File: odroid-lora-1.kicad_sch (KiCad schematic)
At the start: 14 parts, among them J1 ODROID_2x12_GPIO, J2 RASPPI_2x20_GPIO, J3 M0, J4 M1

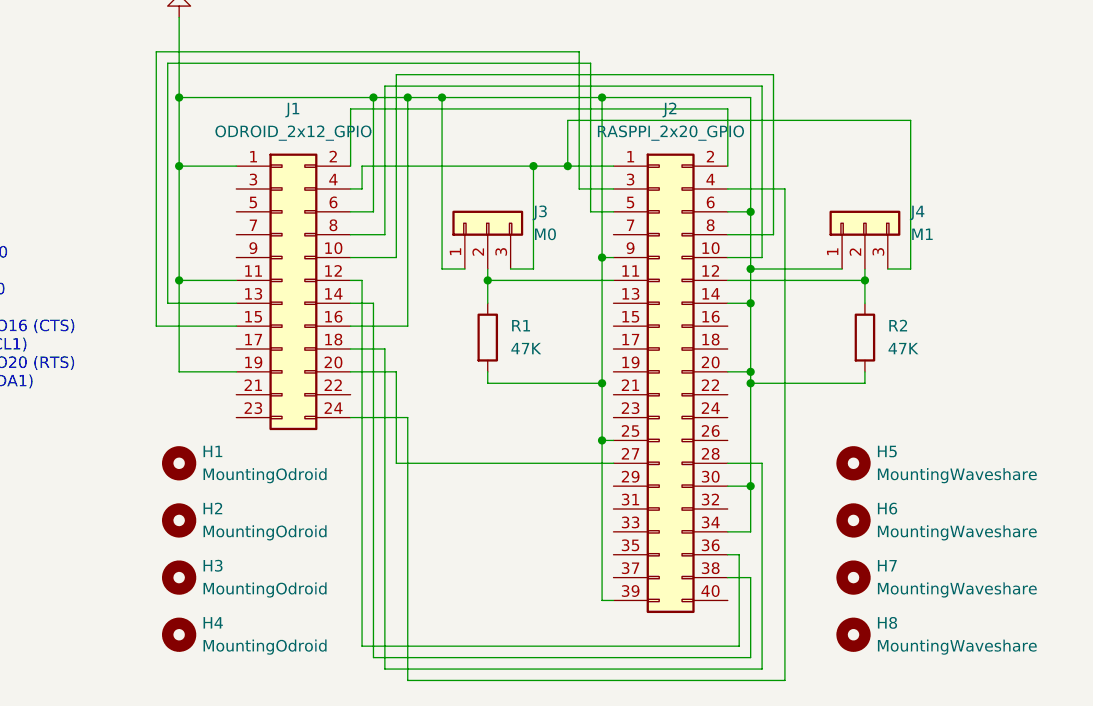
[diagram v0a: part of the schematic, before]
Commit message: update to angled condensed design
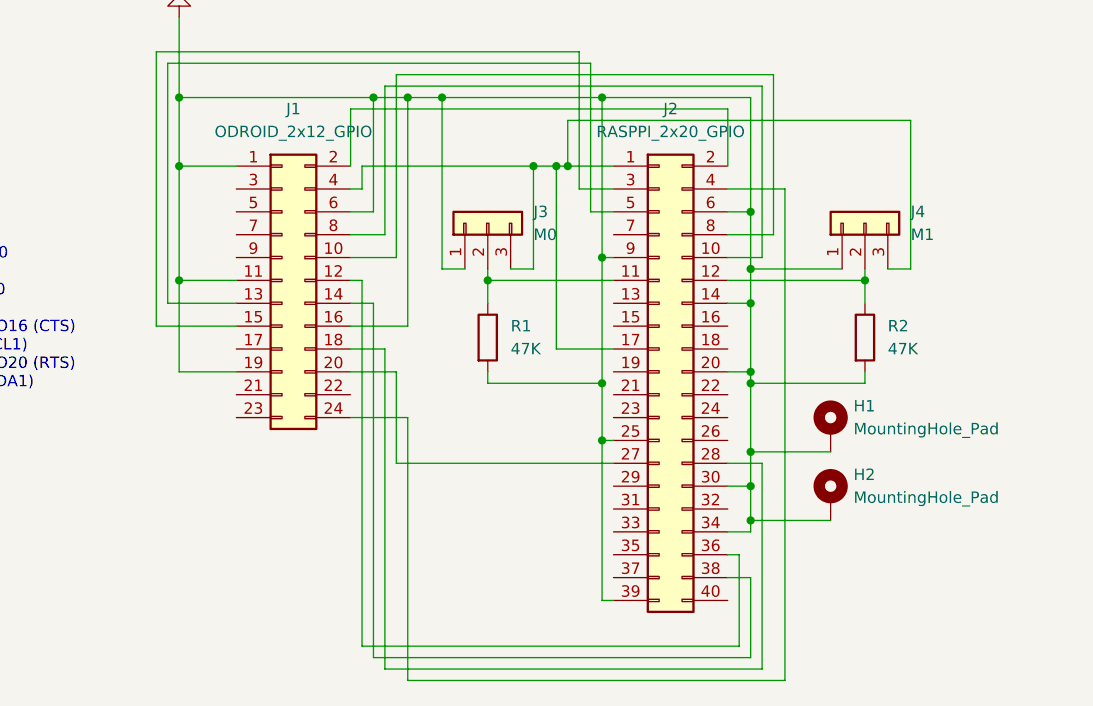
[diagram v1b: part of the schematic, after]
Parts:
- removed H1, H2, H3, H4: MountingOdroid, MountingHole:MountingHole_3.5mm_Pad, symbol Mechanical:MountingHole
- removed H5, H6, H7, H8: MountingWaveshare, MountingHole:MountingHole_3.5mm_Pad, symbol Mechanical:MountingHole
- added H1, H2: MountingHole_Pad, MountingHole:MountingHole_3.5mm_Pad, symbol Mechanical:MountingHole_Pad
- J1: footprint Connector_PinHeader_2.54mm:PinHeader_2x12_P2.54mm_Vertical -> Connector_PinHeader_2.54mm:PinHeader_2x12_P2.54mm_Horizontal
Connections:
- net GND: now also H1.1, H2.1
- net at J1.4 (Pin_4), J2.1 (Pin_1), J3.3 (Pin_3)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: now also J2.17 (Pin_17)

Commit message: replace pinheader with pinsocket for the odroid connector
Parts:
- J1: footprint Connector_PinHeader_2.54mm:PinHeader_2x12_P2.54mm_Horizontal -> Connector_PinSocket_2.54mm:PinSocket_2x12_P2.54mm_Horizontal
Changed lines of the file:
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@@
 			)
 		)
-		(property "Footprint" "Connector_PinHeader_2.54mm:PinHeader_2x12_P2.54mm_Horizontal"
+		(property "Footprint" "Connector_PinSocket_2.54mm:PinSocket_2x12_P2.54mm_Horizontal"
 			(at 116.84 78.74 0)
 			(effects

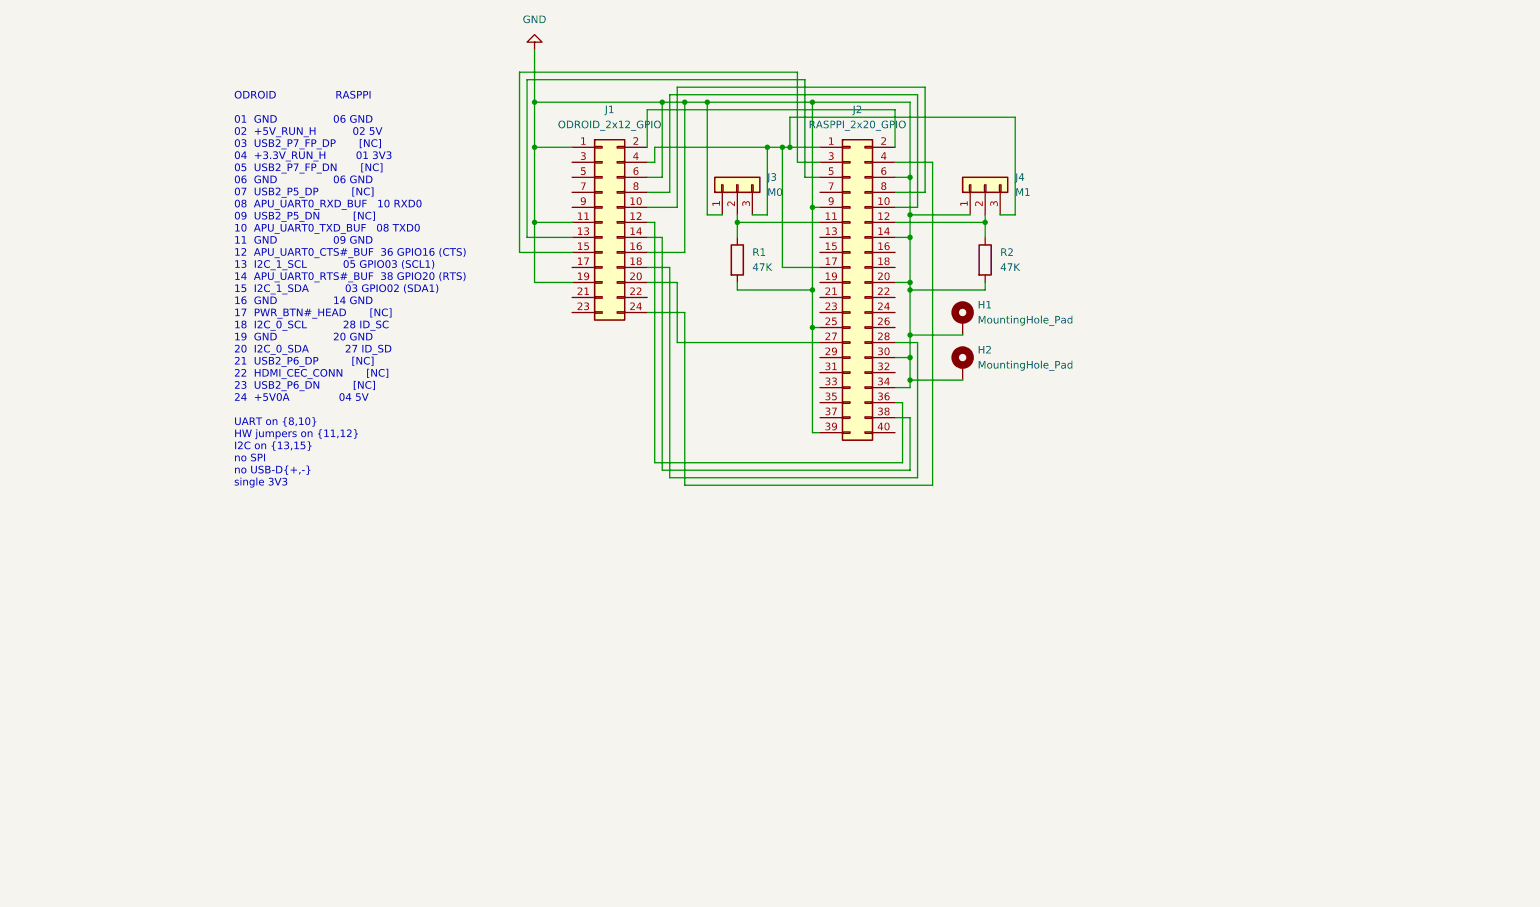
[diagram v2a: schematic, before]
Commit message: define power nets and increase trace width for currents
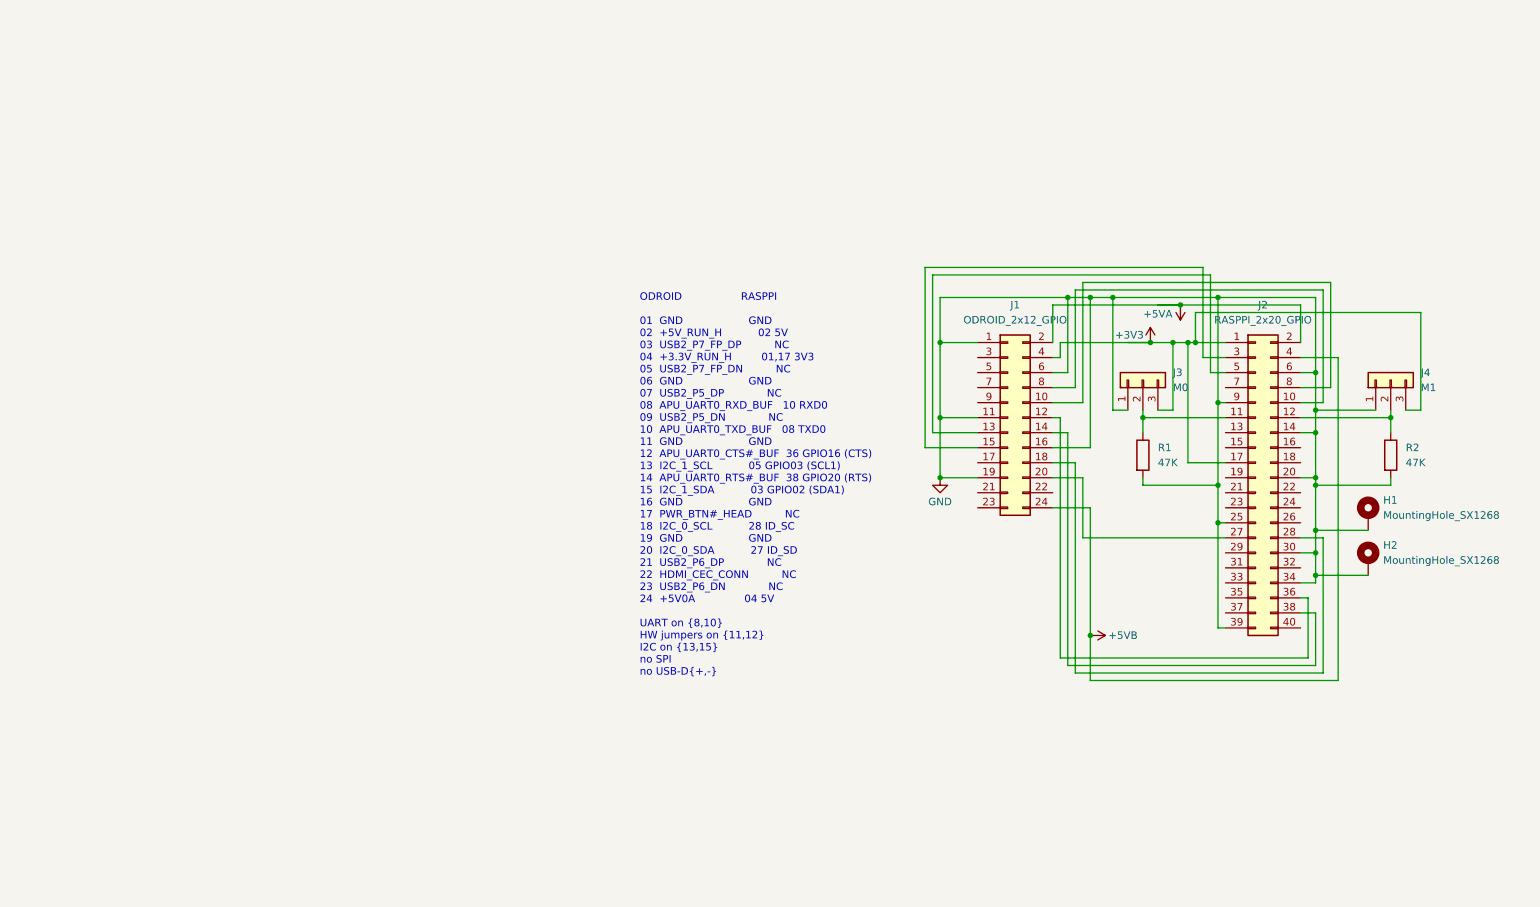
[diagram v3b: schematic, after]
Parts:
- H1, H2: value MountingHole_Pad -> MountingHole_SX1268
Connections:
- net +3V3: now reaches J1.4 (Pin_4), J2.1 (Pin_1), J2.17 (Pin_17), J3.3 (Pin_3), J4.3 (Pin_3)
- net +5VA: now reaches J1.2 (Pin_2), J2.2 (Pin_2)
- net +5VB: now reaches J1.24 (Pin_24), J2.4 (Pin_4)
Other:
- note added: "ODROID RASPPI 01 GND GND 02 +5V_RUN_H 02 5V 03 USB2_P7_FP_DP NC 04 +3.3V_RUN_H 01,17 3V3 05 USB2_P7_FP_DN NC 06 GND GND 07 USB2_P5_DP NC 08 APU_UART0_RXD_BUF 10 RXD0 09 USB2_P5_DN NC 10 APU_UART0_TXD_BUF 08 TXD0 11 GND GND 12 APU_UART0_CTS#_BUF 36 GPIO16 (CTS) 13 I2C_1_SCL 05 GPIO03 (SCL1) 14 APU_UART0_RTS#_BUF 38 GPIO20 (RTS) 15 I2C_1_SDA 03 GPIO02 (SDA1) 16 GND GND 17 PWR_BTN#_HEAD NC 18 I2C_0_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"
- note removed: "ODROID RASPPI 01 GND 06 GND 02 +5V_RUN_H 02 5V 03 USB2_P7_FP_DP [NC] 04 +3.3V_RUN_H 01 3V3 05 USB2_P7_FP_DN [NC] 06 GND 06 GND 07 USB2_P5_DP [NC] 08 APU_UART0_RXD_BUF 10 RXD0 09 USB2_P5_DN [NC] 10 APU_UART0_TXD_BUF 08 TXD0 11 GND 09 GND 12 APU_UART0_CTS#_BUF 36 GPIO16 (CTS) 13 I2C_1_SCL 05 GPIO03 (SCL1) 14 APU_UART0_RTS#_BUF 38 GPIO20 (RTS) 15 I2C_1_SDA 03 GPIO02 (SDA1) 16 GND 14 GND 17 PWR_BTN#_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"
- company: (none) -> l5yth
- title: (none) -> odroid-h3-sx1268-lora-hat
- moved on the sheet: H1, H2, J1, J2, J3, J4, R1, R2

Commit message: add fuses
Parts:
- added F1, F2: Fuse_2A, Fuse:Fuse_1206_3216Metric, symbol Device:Fuse
- H1, H2: value MountingHole_SX1268 -> MOUNT_SX1268
- J1: value ODROID_2x12_GPIO -> ODROID_2x12_SOCKET
- J2: value RASPPI_2x20_GPIO -> RASPPI_2x20_HEADER
- J3: value M0 -> Mode0
- J4: value M1 -> Mode1
- R1, R2: value 47K -> 51K
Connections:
- net GPIO_M0: now reaches J2.11 (Pin_11), J3.2 (Pin_2), R1.1
- net GPIO_M1: now reaches J2.12 (Pin_12), J4.2 (Pin_2), R2.1
- net UART0_RXD: now reaches J1.8 (Pin_8), J2.10 (Pin_10)
- net I2C0_SDA: now reaches J1.20 (Pin_20), J2.27 (Pin_27)
- net I2C0_SCL: now reaches J1.18 (Pin_18), J2.28 (Pin_28)
- net I2C1_SDA: now reaches J1.15 (Pin_15), J2.3 (Pin_3)
- net UART0_CTS: now reaches J1.12 (Pin_12), J2.36 (Pin_36)
- net UART0_RTS: now reaches J1.14 (Pin_14), J2.38 (Pin_38)
- net I2C1_SCL: now reaches J1.13 (Pin_13), J2.5 (Pin_5)
- net UART0_TXD: now reaches J1.10 (Pin_10), J2.8 (Pin_8)
- net +3V3 renamed 3V_RUN_H
- net 3V_RUN_H: now also F2.1, F2.2
- net +5VA renamed 5V_RUN_H
- net 5V_RUN_H: now also J2.4 (Pin_4), F1.1, F1.2
- net +5VB: no longer names the net of J1.24 (Pin_24)
- net +5VB: no longer J2.4 (Pin_4)
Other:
- note added: "ODROID RASPPI 01 GND GND 02 +5V_RUN_H 02,04 5V 03 USB2_P7_FP_DP NC 04 +3.3V_RUN_H 01,17 3V3 05 USB2_P7_FP_DN NC 06 GND GND 07 USB2_P5_DP NC 08 APU_UART0_RXD_BUF 10 RXD0 09 USB2_P5_DN NC 10 APU_UART0_TXD_BUF 08 TXD0 11 GND GND 12 APU_UART0_CTS#_BUF 36 GPIO16 (CTS) 13 I2C_1_SCL 05 GPIO03 (SCL1) 14 APU_UART0_RTS#_BUF 38 GPIO20 (RTS) 15 I2C_1_SDA 03 GPIO02 (SDA1) 16 GND GND 17 PWR_BTN#_HEAD NC 18 I2C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"
- note removed: "ODROID RASPPI 01 GND GND 02 +5V_RUN_H 02 5V 03 USB2_P7_FP_DP NC 04 +3.3V_RUN_H 01,17 3V3 05 USB2_P7_FP_DN NC 06 GND GND 07 USB2_P5_DP NC 08 APU_UART0_RXD_BUF 10 RXD0 09 USB2_P5_DN NC 10 APU_UART0_TXD_BUF 08 TXD0 11 GND GND 12 APU_UART0_CTS#_BUF 36 GPIO16 (CTS) 13 I2C_1_SCL 05 GPIO03 (SCL1) 14 APU_UART0_RTS#_BUF 38 GPIO20 (RTS) 15 I2C_1_SDA 03 GPIO02 (SDA1) 16 GND GND 17 PWR_BTN#_HEAD NC 18 I2C_0_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"
- moved on the sheet: H1, H2, J1, J2, J3, J4, R1, R2
